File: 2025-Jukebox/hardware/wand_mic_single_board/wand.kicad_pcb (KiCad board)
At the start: 4 copper layers, 17.5 x 64 mm, 52 parts, among them J1 USB_C_Receptacle_USB2.0, J4 Conn_01x02, J9 Conn_01x02, Q1 MUN5214DW1T1G, Q3 CJ3139K, SW1 SW_Push, U1 CP2104, U2 ESP32-PICO-D4, U3 ICM-20948, U4 TP4065-4.2V, U5 TLV76718DRVx, U6 LY68L6400SLIT, U7 PCA9306, U9 TLV76733DRVx

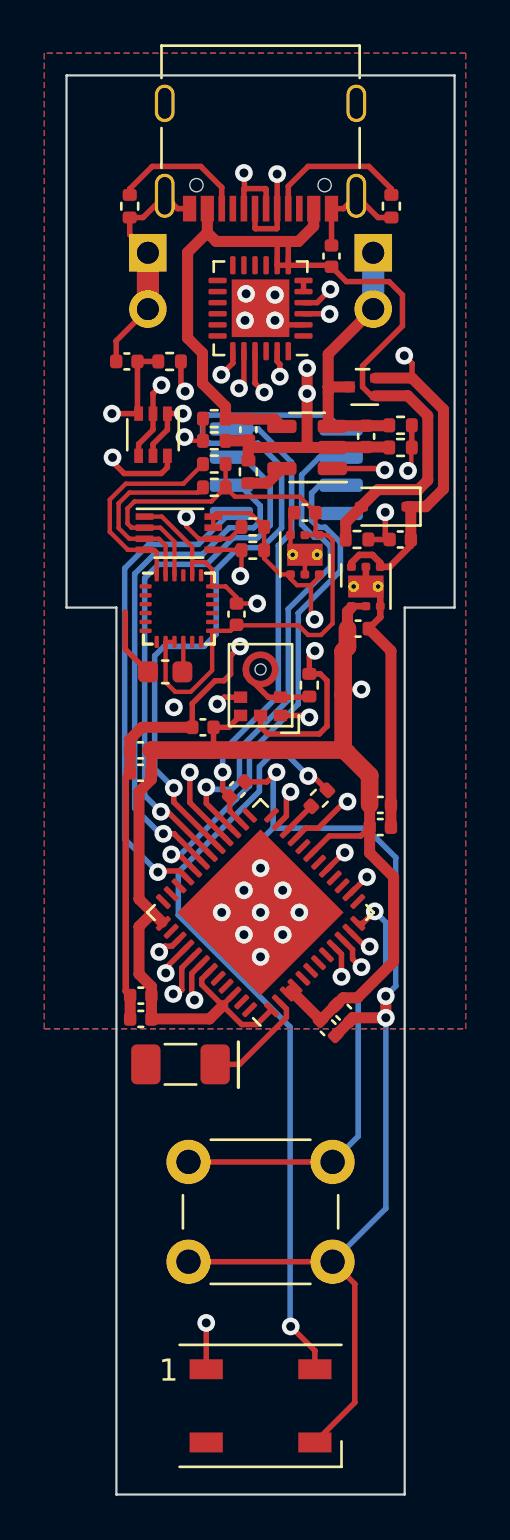
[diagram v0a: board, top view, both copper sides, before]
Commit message: Added footprint for light pipe
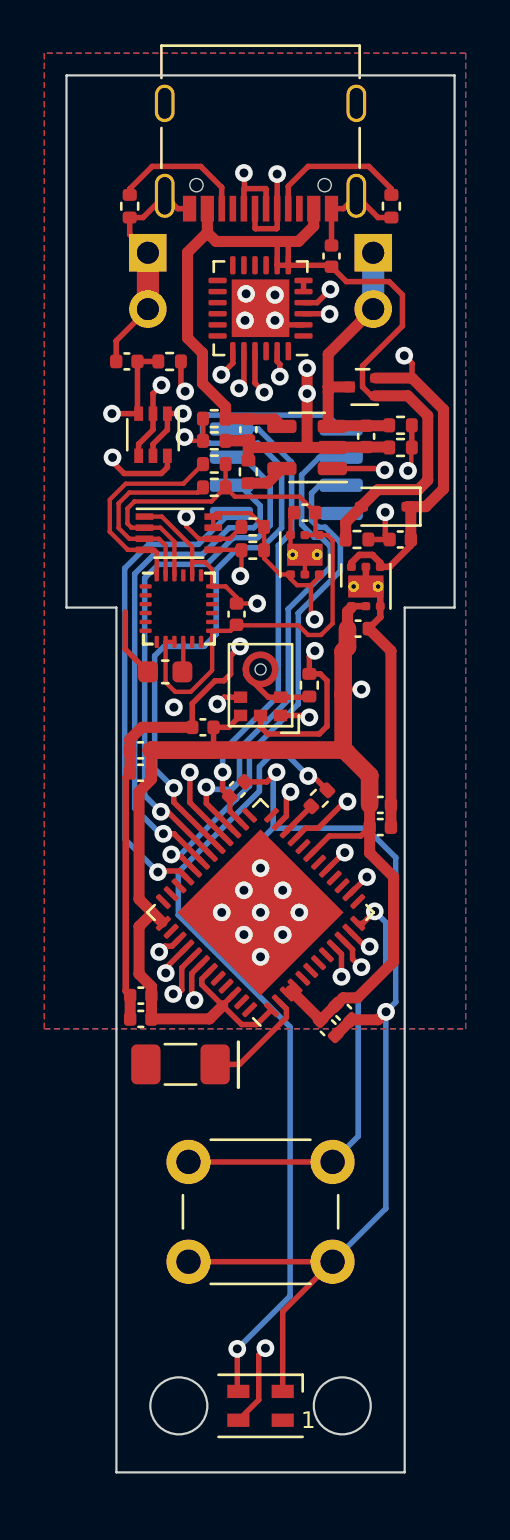
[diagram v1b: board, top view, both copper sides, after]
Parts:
- D2: value WS2812B -> SK6805; footprint LED_SMD:LED_WS2812B_PLCC4_5.0x5.0mm_P3.2mm -> LED_SMD:LED_SK6805_PLCC4_2.4x2.7mm_P1.3mm
- turned D2 to 180 degrees
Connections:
- D2 pad 1: PWR_4V5_5V -> unconnected-(D2-DOUT-Pad1)
- D2 pad 2: unconnected-(D2-DOUT-Pad2) -> GND
- D2 pad 3: GND -> Net-(D2-DIN)
- D2 pad 4: Net-(D2-DIN) -> PWR_4V5_5V
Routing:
- net GND: track 178.5 -> 176.8 mm, vias 22 -> 21
- net PWR_4V5_5V: track 83.0 -> 84.7 mm
- net Net-(D2-DIN): track 35.1 -> 36.7 mm
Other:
- board size 17.5 x 64 mm -> 17.5 x 63 mm
